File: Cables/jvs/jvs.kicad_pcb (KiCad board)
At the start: 2 copper layers, 40 x 18.5 mm, 19 parts, among them J1 DB25_Male, J2 Conn_01x01, J3 Conn_01x01, J4 Conn_01x01, J5 Conn_01x01, U1 THVD1450, U2 TPS6124x, U3 74AHC1G125

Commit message: Tweak for JVS PCB
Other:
- board text added: "(2-D-) B"
- board text added: "A (3-D+)"
- board text added: "GND (4-GND)"
- board text added: "SENSE (1-VBUS)"
- board text added: "SU"
- board text added: "VIN"
- board text removed: "A (D+)"
- board text removed: "B (D-)"
- board text removed: "GND"
- board text removed: "SENSE"

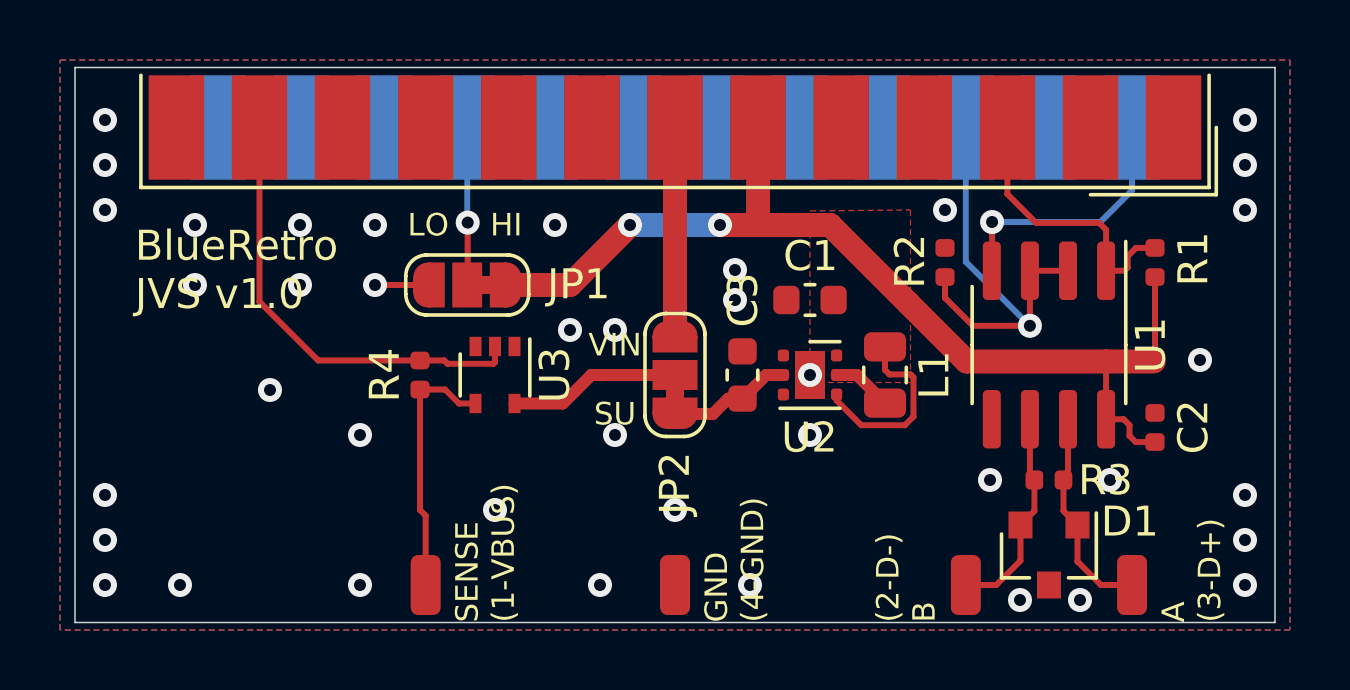
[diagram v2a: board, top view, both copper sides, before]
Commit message: [JVS] Fixup Step Up feedback wiring
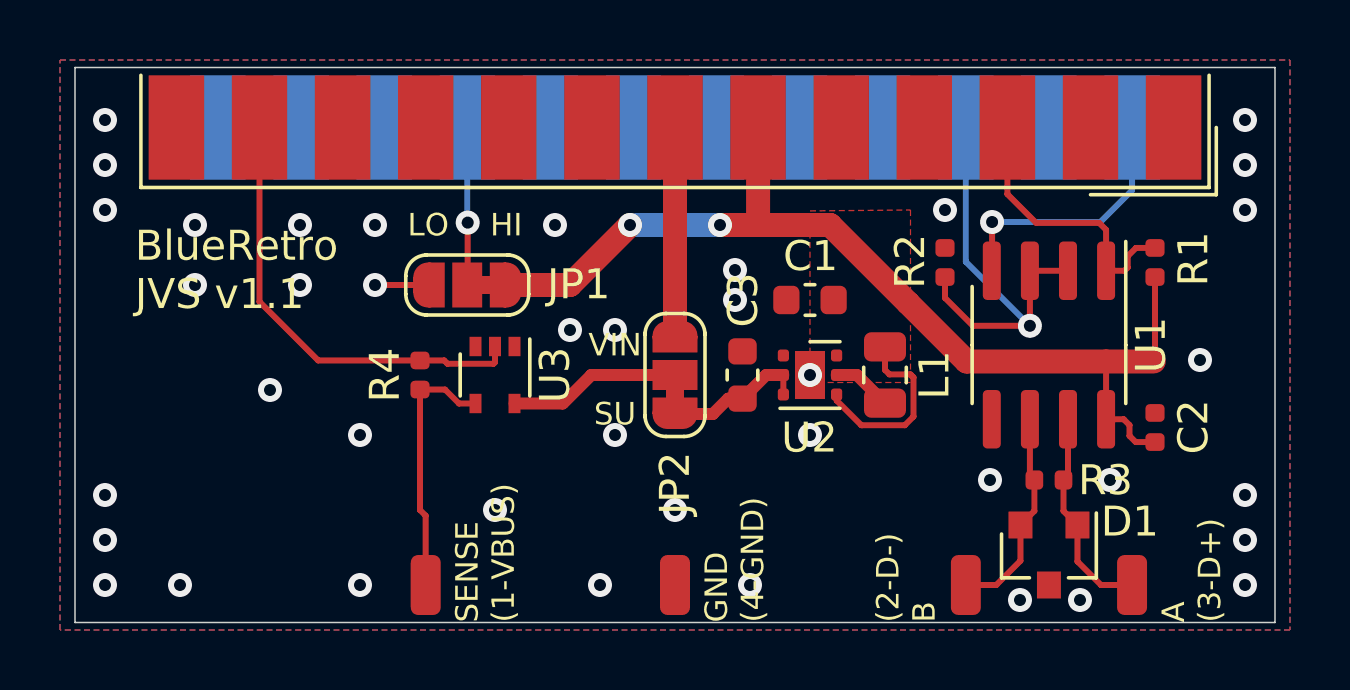
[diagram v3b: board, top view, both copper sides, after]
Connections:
- U2 pad 3: /GND -> /5V_SU
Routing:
- net /5V_SU: track 4.15 -> 4.80 mm
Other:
- board text added: "BlueRetro JVS v1.1"
- board text removed: "BlueRetro JVS v1.0"
